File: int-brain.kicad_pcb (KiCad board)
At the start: 2 copper layers, 152.4 x 66.5 mm, 102 parts, among them J1 PWR, J10 Left, J11 Right, J12 1MA_ENC, J13 1MB_ENC, J14 2MA_ENC, J15 2MB_ENC, J16 USB_A, J2 UART0, J3 I2C0, J4 PWR, J5 1MA, J6 1MB, J7 2MA, J8 2MB, J9 MPU9250, SW1 SW_Push, U1 L298N, U2 ESP32-DevKitC, U3 L298N, U4 TPS5430DDA, U7 PCA9635, U8 TPS5430DDA

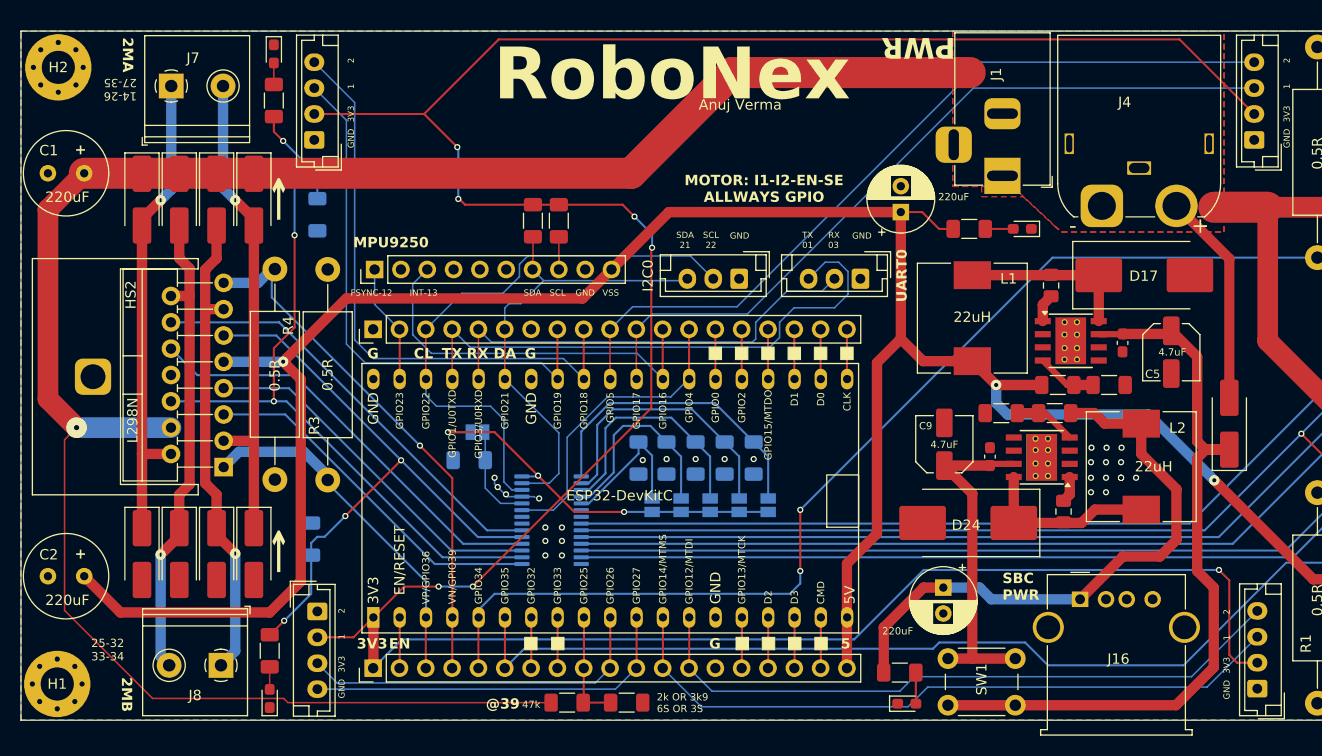
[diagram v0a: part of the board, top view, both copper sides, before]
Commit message: add cap to PCA ic
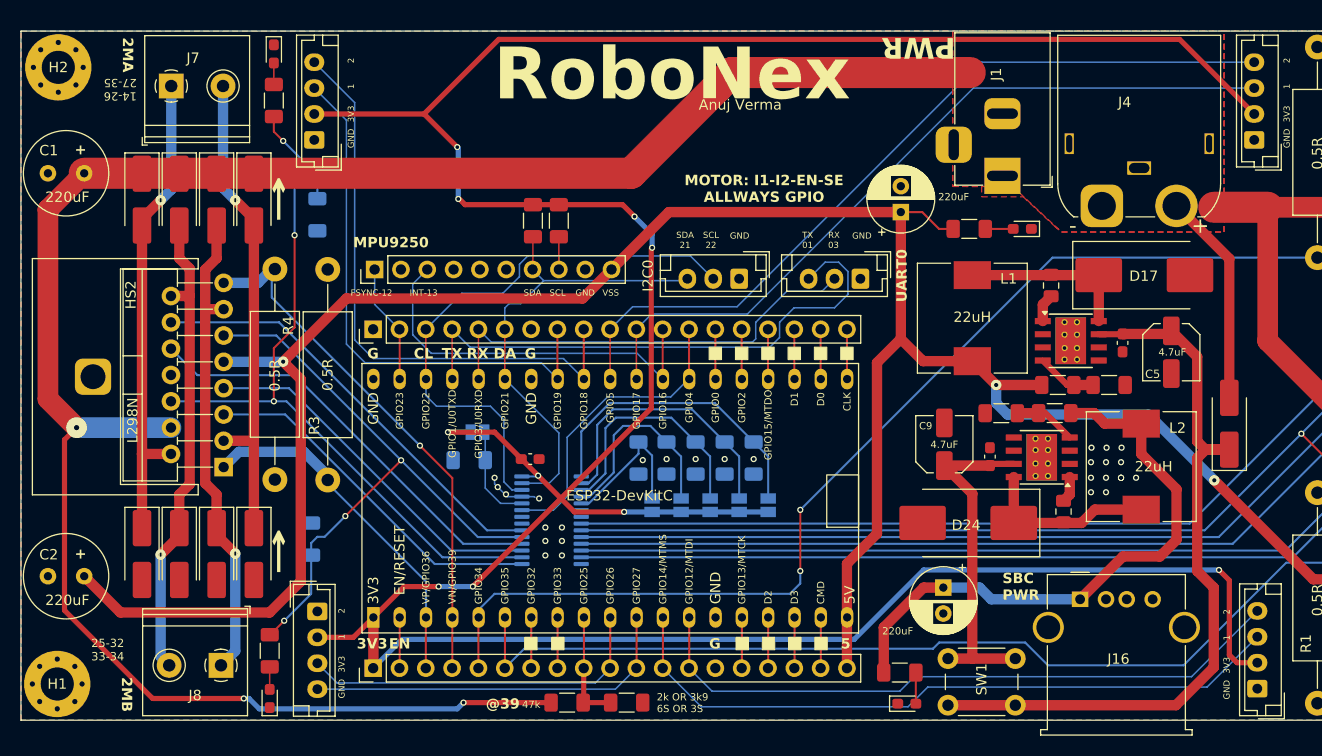
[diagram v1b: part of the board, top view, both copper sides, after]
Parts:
- added C13: 100nF, Capacitor_SMD:C_0603_1608Metric_Pad1.08x0.95mm_HandSolder, F.Cu at (167.0, 94.8)
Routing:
- net VS: track 290.8 -> 291.3 mm, vias 2 -> 4

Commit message: some zone
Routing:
- net VS: track 291.3 -> 289.0 mm
- net +3.3V: track 324.5 -> 322.6 mm
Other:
- outline, holes or cut-outs redrawn
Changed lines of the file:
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@@
 		(tags "capacitor handsolder")
 		(property "Reference" "C13"
-			(at 0 -1.43 360)
+			(at 0 -1.43 0)
 			(layer "F.SilkS")
 			(hide yes)
@@
 		)
 		(property "Value" "100nF"
-			(at 0 1.43 360)
+			(at 0 1.43 0)
 			(layer "F.Fab")
 			(effects
@@
 		)
 		(fp_text user "${REFERENCE}"
-			(at 0 0 360)
+			(at 0 0 0)
 			(layer "F.Fab")
 			(effects
@@
 		)
 		(property "Value" "1MA"
-			(at 8.95 -2.75 90)
+			(at 8.95 -1.9 90)
 			(unlocked yes)
 			(layer "F.SilkS" knockout)
@@
 		(layer "F.SilkS")
 	)
-	(gr_rect
-		(start 117.9 53.5)
-		(end 270.3 120)
+	(gr_arc
+		(start 268.3 53.5)
+		(mid 269.714214 54.085786)
+		(end 270.3 55.5)
+		(stroke
+			(width 0.05)
+			(type default)
+		)
+		(layer "Edge.Cuts")
+	)
+	(gr_line
+		(start 270.3 55.5)
+		(end 270.3 118)
+		(stroke
+			(width 0.05)
+			(type default)
+		)
+		(layer "Edge.Cuts")
+	)
+	(gr_line
+		(start 268.3 120)
+		(end 119.9 120)
+		(stroke
+			(width 0.05)
+			(type default)
+		)
+		(layer "Edge.Cuts")
+	)
+	(gr_line
+		(start 119.9 53.5)
+		(end 268.3 53.5)
+		(stroke
+			(width 0.05)
+			(type default)
+		)
+		(layer "Edge.Cuts")
+	)
+	(gr_arc
+		(start 119.9 120)
+		(mid 118.485786 119.414214)
+		(end 117.9 118)
+		(stroke
+			(width 0.05)
+			(type default)
+		)
+		(layer "Edge.Cuts")
+	)
+	(gr_line
+		(start 117.9 118)
+		(end 117.9 55.5)
+		(stroke
+			(width 0.05)
+			(type default)
+		)
+		(layer "Edge.Cuts")
+	)
+	(gr_arc
+		(start 270.3 118)
+		(mid 269.714214 119.414214)
+		(end 268.3 120)
+		(stroke
+			(width 0.05)
+			(type default)
+		)
+		(layer "Edge.Cuts")
+	)
+	(gr_arc
+		(start 117.9 55.5)
+		(mid 118.485786 54.085786)
+		(end 119.9 53.5)
 		(stroke
 			(width 0.05)
 			(type default)
 		)
-		(fill none)
 		(layer "Edge.Cuts")
 	)
@@
 	)
 	(segment
-		(start 186.5 57.5)
-		(end 209.5 57.5)
-		(width 3)
+		(start 160.6 118.3)
+		(end 169.05 118.3)
+		(width 0.5)
 		(layer "F.Cu")
 		(net 1)
@@
 	(segment
 		(start 176.78 67.22)
-		(end 185 59)
+		(end 184.4 59.6)
 		(width 3)
 		(layer "F.Cu")
@@
 	)
 	(segment
-		(start 160.6 118.3)
-		(end 169.05 118.3)
-		(width 0.5)
-		(layer "F.Cu")
-		(net 1)
-	)
-	(segment
 		(start 124 67.22)
 		(end 176.78 67.22)
@@
 	)
 	(segment
-		(start 185 59)
-		(end 186.5 57.5)
-		(width 3)
-		(layer "F.Cu")
-		(net 1)
-	)
-	(segment
 		(start 238.2 83.4)
 		(end 238.2 70.5)
@@
 	)
 	(segment
+		(start 184.4 59.6)
+		(end 208.1 59.6)
+		(width 3)
+		(layer "F.Cu")
+		(net 1)
+	)
+	(segment
 		(start 255.2 91.8)
 		(end 246.6 91.8)
@@
 	)
 	(segment
-		(start 236.9 61.5)
-		(end 229.7 54.3)
-		(width 0.5)
-		(layer "F.Cu")
-		(net 27)
-	)
-	(segment
 		(start 170 98.6)
 		(end 161.5 107.1)
@@
 	)
 	(segment
-		(start 229.7 54.3)
-		(end 164 54.3)
-		(width 0.5)
-		(layer "F.Cu")
-		(net 27)
-	)
-	(segment
 		(start 169.8 70.25)
 		(end 175.95 70.25)
@@
 	)
 	(segment
+		(start 161.7 56.6)
+		(end 156.8 61.5)
+		(width 0.5)
+		(layer "F.Cu")
+		(net 27)
+	)
+	(segment
 		(start 235.25 114.45)
 		(end 234.5 113.7)
@@
 	)
 	(segment
-		(start 159.1 92.2)
-		(end 163.6 92.2)
+		(start 236.9 61.5)
+		(end 232 56.6)
 		(width 0.5)
 		(layer "F.Cu")
@@
 	)
 	(segment
-		(start 160.75 70.25)
-		(end 169.8 70.25)
+		(start 159.1 92.2)
+		(end 163.6 92.2)
 		(width 0.5)
 		(layer "F.Cu")
@@
 	)
 	(segment
-		(start 164 54.3)
-		(end 156.8 61.5)
+		(start 160.75 70.25)
+		(end 169.8 70.25)
 		(width 0.5)
 		(layer "F.Cu")
@@
 		(width 0.5)
 		(layer "F.Cu")
+		(net 27)
+	)
+	(segment
+		(start 232 56.6)
+		(end 161.7 56.6)
+		(width 0.5)
+		(layer "F.Cu")

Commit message: add solder point for PCA I/O
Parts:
- added JP6: VCC, Jumper:SolderJumper-2_P1.3mm_Open_Pad1.0x1.5mm, F.Cu at (162.3, 99.0)
- added JP7: GND, Jumper:SolderJumper-2_P1.3mm_Open_Pad1.0x1.5mm, F.Cu at (159.5, 99.0)
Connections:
- U7 pad 25: GND -> /PCA_IO
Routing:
- net /PCA_IO: track 0.00 -> 6.82 mm, vias 0 -> 1
- net GND: track 5.20 -> 0.00 mm, vias 40 -> 36
- net +3.3V: track 322.6 -> 327.3 mm
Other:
- board text added: "PCA I/O"

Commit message: placed?
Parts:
- removed D11, D12, D13, D14, D15, D16, D23: D, Diode_SMD:D_SMA_Handsoldering
- removed D17, D24: B340, Diode_SMD:D_SMC_Handsoldering
- removed D18, D19, D20, D21: LED, LED_SMD:LED_0603_1608Metric_Pad1.05x0.95mm_HandSolder
- removed D22, D25: PWR, LED_SMD:LED_0603_1608Metric_Pad1.05x0.95mm_HandSolder
- removed HS1, HS2: Heatsink_Pad, heatsink:Heatsink_PI48
- removed JP0: A0, Jumper:SolderJumper-2_P1.3mm_Open_Pad1.0x1.5mm
- added C14: 220uF, Capacitor_SMD:CP_Elec_8x10.5, F.Cu at (47.8, 73.9)
- added C15: 4.7uF, Capacitor_SMD:CP_Elec_4x5.4, F.Cu at (96.6, 77.3)
- added C16: 4.7uF, Capacitor_SMD:C_0603_1608Metric_Pad1.08x0.95mm_HandSolder, B.Cu at (95.7, 79.2)
- added C17: 10nF, Capacitor_SMD:C_0805_2012Metric_Pad1.18x1.45mm_HandSolder, F.Cu at (104.4, 83.7)
- added C18: 330uF, Capacitor_SMD:CP_Elec_8x10.5, F.Cu at (73.2, 77.8)
- added C19: 10nF, Capacitor_SMD:C_0805_2012Metric_Pad1.18x1.45mm_HandSolder, B.Cu at (134.4, 131.8)
- added C20: 1uF, Capacitor_SMD:C_0805_2012Metric_Pad1.18x1.45mm_HandSolder, B.Cu at (134.4, 136.8)
- added C21: 220uF, Capacitor_SMD:CP_Elec_8x10.5, F.Cu at (119.1, 140.9)
- added C22: 10nF, Capacitor_SMD:C_0603_1608Metric_Pad1.08x0.95mm_HandSolder, B.Cu at (78.0, 132.7)
- added C23: 10nF, Capacitor_SMD:C_0603_1608Metric_Pad1.08x0.95mm_HandSolder, B.Cu at (97.6, 79.2)
- added C24: 10nF, Capacitor_SMD:C_0603_1608Metric_Pad1.08x0.95mm_HandSolder, F.Cu at (107.2, 131.4)
- added C25: 10nF, Capacitor_SMD:C_0603_1608Metric_Pad1.08x0.95mm_HandSolder, F.Cu at (67.8, 80.5)
- added J17: Conn_01x03, Connector_PinHeader_2.54mm:PinHeader_1x03_P2.54mm_Vertical, F.Cu at (63.3, 111.1)
- added R29: 10k, Resistor_SMD:R_1206_3216Metric_Pad1.30x1.75mm_HandSolder, F.Cu at (78.8, 100.0)
- added R30: 3k9, Resistor_SMD:R_1206_3216Metric_Pad1.30x1.75mm_HandSolder, F.Cu at (63.3, 116.0)
- added U10: ~, Package_SO:SOIC-8-1EP_3.9x4.9mm_P1.27mm_EP2.29x3mm_ThermalVias, F.Cu at (103.0, 79.5)
- added U11: DRV8251ADDAR, Package_SO:SOIC-8-1EP_3.9x4.9mm_P1.27mm_EP2.29x3mm_ThermalVias, B.Cu at (130.4, 135.3)
- added U12: INA139, Package_TO_SOT_SMD:SOT-23-5_HandSoldering, B.Cu at (125.3, 136.7)
- added U5: DRV8251ADDAR, Package_SO:SOIC-8-1EP_3.9x4.9mm_P1.27mm_EP2.29x3mm_ThermalVias, B.Cu at (132.2, 79.6)
- added U6: INA139, Package_TO_SOT_SMD:SOT-23-5_HandSoldering, B.Cu at (137.2, 78.3)
- added U9: INA139, Package_TO_SOT_SMD:SOT-23-5_HandSoldering, B.Cu at (62.7, 78.1)
- C1: value 220uF -> 100nF; footprint Capacitor_THT:C_Radial_D8.0mm_H11.5mm_P3.50mm -> Capacitor_SMD:C_0603_1608Metric_Pad1.08x0.95mm_HandSolder; moved to B.Cu
- C10: value 4.7uF -> 10nF; footprint Capacitor_SMD:C_0603_1608Metric_Pad1.08x0.95mm_HandSolder -> Capacitor_SMD:C_0805_2012Metric_Pad1.18x1.45mm_HandSolder
- C11: value 10nF -> 330uF; footprint Capacitor_SMD:C_0805_2012Metric_Pad1.18x1.45mm_HandSolder -> Capacitor_SMD:CP_Elec_8x10.5
- C12: value 220uF -> 10nF; footprint Capacitor_THT:CP_Radial_D6.3mm_P2.50mm -> Capacitor_SMD:C_0805_2012Metric_Pad1.18x1.45mm_HandSolder; moved to B.Cu
- C13: value 100nF -> 1uF; footprint Capacitor_SMD:C_0603_1608Metric_Pad1.08x0.95mm_HandSolder -> Capacitor_SMD:C_0805_2012Metric_Pad1.18x1.45mm_HandSolder; moved to B.Cu
- C2: value 220uF -> 10nF; footprint Capacitor_THT:C_Radial_D8.0mm_H11.5mm_P3.50mm -> Capacitor_SMD:C_0805_2012Metric_Pad1.18x1.45mm_HandSolder; moved to B.Cu
- C3: value 220uF -> 1uF; footprint Capacitor_THT:C_Radial_D8.0mm_H11.5mm_P3.50mm -> Capacitor_SMD:C_0805_2012Metric_Pad1.18x1.45mm_HandSolder; moved to B.Cu
- C4: footprint Capacitor_THT:C_Radial_D8.0mm_H11.5mm_P3.50mm -> Capacitor_SMD:CP_Elec_8x10.5
- C5: value 4.7uF -> 10nF; footprint Capacitor_SMD:C_Elec_5x5.8 -> Capacitor_SMD:C_0805_2012Metric_Pad1.18x1.45mm_HandSolder; moved to B.Cu
- C6: value 4.7uF -> 1uF; footprint Capacitor_SMD:C_0603_1608Metric_Pad1.08x0.95mm_HandSolder -> Capacitor_SMD:C_0805_2012Metric_Pad1.18x1.45mm_HandSolder; moved to B.Cu
- C7: value 10nF -> 220uF; footprint Capacitor_SMD:C_0805_2012Metric_Pad1.18x1.45mm_HandSolder -> Capacitor_SMD:CP_Elec_8x10.5
- C8: value 220uF -> 4.7uF; footprint Capacitor_THT:CP_Radial_D6.3mm_P2.50mm -> Capacitor_SMD:CP_Elec_4x5.4
- C9: footprint Capacitor_SMD:C_Elec_5x5.8 -> Capacitor_SMD:C_0603_1608Metric_Pad1.08x0.95mm_HandSolder; moved to B.Cu
- D1, D2, D3, D4: value D -> LED; footprint Diode_SMD:D_SMA_Handsoldering -> LED_SMD:LED_1206_3216Metric_Pad1.42x1.75mm_HandSolder
- D6, D7: value D -> PWR; footprint Diode_SMD:D_SMA_Handsoldering -> LED_SMD:LED_1206_3216Metric_Pad1.42x1.75mm_HandSolder
- D8, D9: value D -> SS54
- J1: value PWR -> Right; footprint Connector_BarrelJack:BarrelJack_Horizontal -> Connector_PinHeader_2.54mm:PinHeader_1x19_P2.54mm_Vertical
- J10: value Left -> 2MB; footprint Connector_PinHeader_2.54mm:PinHeader_1x19_P2.54mm_Vertical -> TerminalBlock_Philmore:TerminalBlock_Philmore_TB132_1x02_P5.00mm_Horizontal
- J11: value Right -> 1MB; footprint Connector_PinHeader_2.54mm:PinHeader_1x19_P2.54mm_Vertical -> TerminalBlock_Philmore:TerminalBlock_Philmore_TB132_1x02_P5.00mm_Horizontal
- J12: value 1MA_ENC -> 1MA; footprint Connector_JST:JST_EH_B4B-EH-A_1x04_P2.50mm_Vertical -> TerminalBlock_Philmore:TerminalBlock_Philmore_TB132_1x02_P5.00mm_Horizontal
- J13: value 1MB_ENC -> 1MA_ENC
- J14: value 2MA_ENC -> 1MB_ENC
- J15: value 2MB_ENC -> 2MA_ENC
- J16: value USB_A -> MPU9250; footprint Connector_USB:USB_A_Molex_67643_Horizontal -> Connector_PinHeader_2.54mm:PinHeader_1x10_P2.54mm_Vertical
- J2: value UART0 -> Left; footprint Connector_JST:JST_EH_B3B-EH-A_1x03_P2.50mm_Vertical -> Connector_PinHeader_2.54mm:PinHeader_1x19_P2.54mm_Vertical
- J3: value I2C0 -> PWR; footprint Connector_JST:JST_EH_B3B-EH-A_1x03_P2.50mm_Vertical -> Connector_BarrelJack:BarrelJack_Horizontal
- J5: value 1MA -> USB_A; footprint TerminalBlock_Philmore:TerminalBlock_Philmore_TB132_1x02_P5.00mm_Horizontal -> Connector_USB:USB_A_Molex_67643_Horizontal
- J6: value 1MB -> 2MB_ENC; footprint TerminalBlock_Philmore:TerminalBlock_Philmore_TB132_1x02_P5.00mm_Horizontal -> Connector_JST:JST_EH_B4B-EH-A_1x04_P2.50mm_Vertical
- J7: value 2MA -> I2C0; footprint TerminalBlock_Philmore:TerminalBlock_Philmore_TB132_1x02_P5.00mm_Horizontal -> Connector_JST:JST_EH_B3B-EH-A_1x03_P2.50mm_Vertical
- J8: value 2MB -> UART0; footprint TerminalBlock_Philmore:TerminalBlock_Philmore_TB132_1x02_P5.00mm_Horizontal -> Connector_JST:JST_EH_B3B-EH-A_1x03_P2.50mm_Vertical
- J9: value MPU9250 -> 2MA; footprint Connector_PinHeader_2.54mm:PinHeader_1x10_P2.54mm_Vertical -> TerminalBlock_Philmore:TerminalBlock_Philmore_TB132_1x02_P5.00mm_Horizontal
- JP1: value A1 -> A0
- JP2: value A2 -> A1
- JP3: value A3 -> A2
- JP4: value A4 -> A3
- JP5: value A5 -> A4
- JP6: value VCC -> A5; moved to B.Cu
- JP7: value GND -> VCC; moved to B.Cu
- R1, R2, R3: value 0.5R -> 220R; footprint Resistor_THT:R_Axial_DIN0414_L11.9mm_D4.5mm_P20.32mm_Horizontal -> Resistor_SMD:R_1206_3216Metric_Pad1.30x1.75mm_HandSolder
- R10: value 47k -> 3k9
- R12, R21: moved to F.Cu
- R13, R14: value 10k -> 470R; moved to F.Cu
- R15: value 10k -> 4.7k
- R16: moved to B.Cu
- R17: value 4.7k -> 10mR; footprint Resistor_SMD:R_1206_3216Metric_Pad1.30x1.75mm_HandSolder -> Resistor_SMD:R_2512_6332Metric_Pad1.40x3.35mm_HandSolder; moved to B.Cu
- R18, R20, R28: value 10k -> 24k
- R19: value 10k -> 10mR; footprint Resistor_SMD:R_1206_3216Metric_Pad1.30x1.75mm_HandSolder -> Resistor_SMD:R_2512_6332Metric_Pad1.40x3.35mm_HandSolder
- R22: value 10k -> 3.16k; moved to F.Cu
- R23: value 470R -> 10mR; footprint Resistor_SMD:R_1206_3216Metric_Pad1.30x1.75mm_HandSolder -> Resistor_SMD:R_2512_6332Metric_Pad1.40x3.35mm_HandSolder; moved to B.Cu
- R24: value 10k -> 24k; moved to B.Cu
- R25: value 3.24k -> 10k
- R26: value 10k -> 3.16k
- R27: value 3.24k -> 10mR; footprint Resistor_SMD:R_1206_3216Metric_Pad1.30x1.75mm_HandSolder -> Resistor_SMD:R_2512_6332Metric_Pad1.40x3.35mm_HandSolder; moved to B.Cu
- R4: value 0.5R -> 10k; footprint Resistor_THT:R_Axial_DIN0414_L11.9mm_D4.5mm_P20.32mm_Horizontal -> Resistor_SMD:R_1206_3216Metric_Pad1.30x1.75mm_HandSolder
- R6, R7: value 220R -> 10k
- R8: value 220R -> 47k
- R9: value 470R -> 10k
- U1: value L298N -> PCA9635; footprint Package_TO_SOT_THT:TO-220-15_P2.54x2.54mm_StaggerOdd_Lead4.58mm_Vertical -> Package_SO:TSSOP-28_4.4x9.7mm_P0.65mm; moved to B.Cu
- U2: footprint PCM_Espressif:ESP32-DevKitC -> PCM_Espressif:ESP32-DevKitC-slim
- U3: value L298N -> DRV8251ADDAR; footprint Package_TO_SOT_THT:TO-220-15_P2.54x2.54mm_StaggerOdd_Lead4.58mm_Vertical -> Package_SO:SOIC-8-1EP_3.9x4.9mm_P1.27mm_EP2.29x3mm_ThermalVias; moved to B.Cu
- U4: value TPS5430DDA -> INA139; footprint Package_SO:TI_SO-PowerPAD-8_ThermalVias -> Package_TO_SOT_SMD:SOT-23-5_HandSoldering; moved to B.Cu
- U7: value PCA9635 -> ~; footprint Package_SO:TSSOP-28_4.4x9.7mm_P0.65mm -> Package_SO:SOIC-8-1EP_3.9x4.9mm_P1.27mm_EP2.29x3mm_ThermalVias; moved to F.Cu
- U8: value TPS5430DDA -> DRV8251ADDAR; footprint Package_SO:TI_SO-PowerPAD-8_ThermalVias -> Package_SO:SOIC-8-1EP_3.9x4.9mm_P1.27mm_EP2.29x3mm_ThermalVias; moved to B.Cu
- moved J6 227.3 mm to (40.0, 142.4), turned to 90 degrees
- moved D5 223.0 mm to (42.6, 88.3), turned to 0 degrees
- moved C4 214.7 mm to (47.6, 140.9), turned to 90 degrees
- moved D2 208.1 mm to (51.7, 133.0), turned to 180 degrees
- moved D1 206.4 mm to (51.7, 81.7), turned to 0 degrees
- moved R2 205.6 mm to (45.6, 133.0), turned to 0 degrees
- moved D7 201.4 mm to (72.4, 139.3), turned to 180 degrees
- moved R1 198.0 mm to (45.7, 81.7), turned to 180 degrees
- moved H4 193.8 mm to (59.3, 94.0)
- moved C3 192.5 mm to (62.6, 136.8), turned to 90 degrees
- moved H3 189.9 mm to (59.9, 123.9)
- moved R14 188.0 mm to (67.0, 139.3), turned to 0 degrees
- moved U1 181.6 mm to (84.6, 109.7), turned to 180 degrees
- moved D8 180.6 mm to (83.1, 133.0)
- moved R12 178.6 mm to (76.1, 100.0), turned to -90 degrees
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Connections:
- C1 pad 1: GND -> +3.3V
- C1 pad 2: VS -> GND
- C10 pad 1: /buck2/BUCK_VIN -> Net-(U7-BOOT)
- C10 pad 2: GND -> /buck1/BUCK_OUT
- C11 pad 1: Net-(U8-BOOT) -> VSS
- C11 pad 2: /buck2/BUCK_OUT -> GND
- C12 pad 1: /buck2/VOUT -> +3.3V
- C13 pad 1: +3.3V -> VS
- C2 pad 1: GND -> +3.3V
- C2 pad 2: VSS -> GND
- C3 pad 1: GND -> VS
- C3 pad 2: VSS -> GND
- C4 pad 1: GND -> VS
- C4 pad 2: VS -> GND
- C5 pad 1: BUCK_VS -> +3.3V
- C6 pad 1: BUCK_VS -> VS
- C7 pad 1: Net-(U4-BOOT) -> VS
- C7 pad 2: /buck1/BUCK_OUT -> GND
- C8 pad 1: VSS -> VS
- C9 pad 1: /buck2/BUCK_VIN -> VS
- D1 pad 1: VS -> GND
- D1 pad 2: /1MA1 -> /1MAL
- D10 pad 1: /2MA1 -> VS
- D10 pad 2: GND -> /VS_UNSAFE
- D2 pad 1: /1MA1 -> GND
- D2 pad 2: GND -> /1MBL
- D3 pad 1: VS -> GND
- D3 pad 2: /1MA2 -> /2MAL
- D4 pad 1: /1MA2 -> GND
- D4 pad 2: GND -> /2MBL
- D5 pad 2: /1MB1 -> /VS_UNSAFE
- D6 pad 1: /1MB1 -> GND
- D6 pad 2: GND -> /PWR_LED_2
- D7 pad 1: VS -> GND
- D7 pad 2: /1MB2 -> /PWR_LED_1
- D8 pad 1: /1MB2 -> /buck1/BUCK_OUT
- D9 pad 1: VS -> /buck2/BUCK_OUT
- D9 pad 2: /2MA1 -> GND
- J1 pad 1: VS -> GND
- J1 pad 2: GND -> FSYNC
- J1 pad 3: (no net) -> SCL0
- J10 pad 1: +3.3V -> /2MB1
- J10 pad 2: /EN -> /2MB2
- J11 pad 1: GND -> /1MB1
- J11 pad 2: FSYNC -> /1MB2
- J12 pad 1: GND -> /1MA1
- J12 pad 2: +3.3V -> /1MA2
- J13 pad 3: /1MA1_ENC -> /2MA1_ENC
- J13 pad 4: /1MA2_ENC -> /2MA2_ENC
- J14 pad 3: /2MB1_ENC -> /1MA1_ENC
- J14 pad 4: /2MB2_ENC -> /1MA2_ENC
- J15 pad 3: /1MB1_ENC -> /2MB1_ENC
- J15 pad 4: /1MB2_ENC -> /2MB2_ENC
- J16 pad 1: /buck2/VOUT -> FSYNC
- J16 pad 3: unconnected-(J16-D+-Pad3) -> INT
- J16 pad 4: GND -> unconnected-(J16-Pin_4-Pad4)
- J16 pad 5: GND -> unconnected-(J16-Pin_5-Pad5)
- J2 pad 1: GND -> +3.3V
- J2 pad 2: /RX0 -> /EN
- J2 pad 3: /TX0 -> 2MB_SENSE
- J3 pad 1: GND -> /VS_UNSAFE
- J3 pad 2: SCL0 -> GND
- J3 pad 3: SDA0 -> GND
- J4 pad 2: VS -> /VS_UNSAFE
- J5 pad 1: /1MA1 -> /buck2/VOUT
- J5 pad 2: /1MA2 -> unconnected-(J5-D--Pad2)
- J6 pad 1: /1MB1 -> GND
- J6 pad 2: /1MB2 -> +3.3V
- J7 pad 1: /2MA1 -> GND
- J7 pad 2: /2MA2 -> SCL0
- J8 pad 1: /2MB1 -> GND
- J8 pad 2: /2MB2 -> /RX0
- J9 pad 1: FSYNC -> /2MA1
- J9 pad 2: unconnected-(J9-Pin_2-Pad2) -> /2MA2
- JP1 pad 2: /PCA_A1 -> /PCA_A0
- JP2 pad 2: /PCA_A2 -> /PCA_A1
- JP3 pad 2: /PCA_A3 -> /PCA_A2
- JP4 pad 2: /PCA_A4 -> /PCA_A3
- JP5 pad 2: /PCA_A5 -> /PCA_A4
- JP6 pad 2: /PCA_IO -> /PCA_A5
- JP7 pad 1: GND -> +3.3V
- R1 pad 1: 1MA_SENSE -> /1MA_EN
- R1 pad 2: GND -> /1MAL
- R10 pad 1: VS -> /3S
- R10 pad 2: VBATT -> GND
- R11 pad 1: VBATT -> GND
- R11 pad 2: GND -> /PCA_A4
- R12 pad 1: /1MA_EN -> GND
- R12 pad 2: GND -> /PCA_A5
- R13 pad 1: /2MA_EN -> /buck2/VOUT
- R13 pad 2: GND -> /PWR_LED_2
- R14 pad 1: /1MB_EN -> VSS
- R14 pad 2: GND -> /PWR_LED_1
- R15 pad 1: /2MB_EN -> SCL0
- R15 pad 2: GND -> +3.3V
- R16 pad 1: SCL0 -> SDA0
- R17 pad 1: SDA0 -> /motor-driver-2/IPROPI
- R17 pad 2: +3.3V -> GND
- R18 pad 1: GND -> 1MB_SENSE
- R18 pad 2: /PCA_A1 -> GND
- R19 pad 1: GND -> /motor-driver-3/IPROPI
- R19 pad 2: /PCA_A2 -> GND
- R2 pad 1: 1MB_SENSE -> /1MB_EN
- R2 pad 2: GND -> /1MBL
- R20 pad 1: GND -> 2MA_SENSE
- R20 pad 2: /PCA_A3 -> GND
- R21 pad 1: GND -> VSS
- R21 pad 2: /PCA_A4 -> /buck1/BUCK_VSENSE
- R22 pad 1: GND -> /buck1/BUCK_VSENSE
- R22 pad 2: /PCA_A5 -> GND
- R23 pad 1: /buck2/VOUT -> /motor-driver-1/IPROPI
- R23 pad 2: /PWR_LED_2 -> GND
- R24 pad 1: VSS -> 1MA_SENSE
- R24 pad 2: /buck1/BUCK_VSENSE -> GND
- R25 pad 1: /buck1/BUCK_VSENSE -> /buck2/VOUT
- R25 pad 2: GND -> /buck2/BUCK_VSENSE
- R26 pad 1: /buck2/VOUT -> /buck2/BUCK_VSENSE
- R26 pad 2: /buck2/BUCK_VSENSE -> GND
- R27 pad 1: /buck2/BUCK_VSENSE -> /motor-driver-4/IPROPI
- R28 pad 1: GND -> 2MB_SENSE
- R28 pad 2: /PCA_A0 -> GND
- R3 pad 1: 2MB_SENSE -> /2MA_EN
- R3 pad 2: GND -> /2MAL
- R4 pad 1: 2MA_SENSE -> GND
- R4 pad 2: GND -> /PCA_A0
- R5 pad 1: /1MA_EN -> /2MB_EN
- R5 pad 2: /1MAL -> /2MBL
- R6 pad 1: /1MB_EN -> GND
- R6 pad 2: /1MBL -> /PCA_A1
- R7 pad 1: /2MA_EN -> GND
- R7 pad 2: /2MAL -> /PCA_A2
- R8 pad 1: /2MB_EN -> VS
- R8 pad 2: /2MBL -> VBATT
- R9 pad 1: VSS -> GND
- R9 pad 2: /PWR_LED_1 -> /PCA_A3
- U1 pad 1: 1MA_SENSE -> /PCA_A0
- U1 pad 10: /1MB1_IN -> /2MA_IN1
- U1 pad 11: /1MB_EN -> /2MA_IN2
- U1 pad 12: /1MB2_IN -> /2MB_IN1
- U1 pad 13: /1MB1 -> /2MB_IN2
- U1 pad 14: /1MB2 -> GND
- U1 pad 15: 1MB_SENSE -> /1MB_IN1
- U1 pad 2: /1MA1 -> /PCA_A1
- U1 pad 3: /1MA2 -> /PCA_A2
- U1 pad 4: VS -> /PCA_A3
- U1 pad 5: /1MA1_IN -> /PCA_A4
- U1 pad 6: /1MA_EN -> /2MA_EN
- U1 pad 7: /1MA2_IN -> /2MB_EN
- U1 pad 8: GND -> unconnected-(U1-LED2-Pad8)
- U1 pad 9: VSS -> unconnected-(U1-LED3-Pad9)
- U3 pad 1: 2MB_SENSE -> /motor-driver-2/IPROPI
- U3 pad 2: /2MA1 -> /1MB_IN2
- U3 pad 3: /2MA2 -> /1MB_IN1
- U3 pad 4: VS -> +3.3V
- U3 pad 5: /2MA1_IN -> VS
- U3 pad 6: /2MA_EN -> /1MB1
- U3 pad 7: /2MA2_IN -> GND
- U3 pad 8: GND -> /1MB2
- U3 pad 9: VSS -> GND
- U4 pad 1: Net-(U4-BOOT) -> 1MB_SENSE
- U4 pad 2: unconnected-(U4-NC-Pad2) -> GND
- U4 pad 3: unconnected-(U4-NC-Pad3) -> /motor-driver-2/IPROPI
- U4 pad 4: /buck1/BUCK_VSENSE -> GND
- U4 pad 5: unconnected-(U4-EN-Pad5) -> +3.3V
- U7 pad 1: /PCA_A0 -> Net-(U7-BOOT)
- U7 pad 2: /PCA_A1 -> unconnected-(U7-NC-Pad2)
- U7 pad 3: /PCA_A2 -> unconnected-(U7-NC-Pad3)
- U7 pad 4: /PCA_A3 -> /buck1/BUCK_VSENSE
- U7 pad 5: /PCA_A4 -> unconnected-(U7-ENA-Pad5)
- U7 pad 6: unconnected-(U7-LED0-Pad6) -> GND
- U7 pad 7: unconnected-(U7-LED1-Pad7) -> VS
- U7 pad 8: /1MB2_IN -> /buck1/BUCK_OUT
- U7 pad 9: /1MB_EN -> GND
- U8 pad 1: Net-(U8-BOOT) -> /motor-driver-1/IPROPI
- U8 pad 2: unconnected-(U8-NC-Pad2) -> /1MA_IN2
- U8 pad 3: unconnected-(U8-NC-Pad3) -> /1MA_IN1
- U8 pad 4: /buck2/BUCK_VSENSE -> +3.3V
- U8 pad 5: unconnected-(U8-EN-Pad5) -> VS
- U8 pad 6: GND -> /1MA1
- U8 pad 7: /buck2/BUCK_VIN -> GND
- U8 pad 8: /buck2/BUCK_OUT -> /1MA2
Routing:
- net +3.3V: track 327.3 -> 0.00 mm, vias 10 -> 0
- net VS: track 289.0 -> 7.35 mm, vias 4 -> 1
- net VSS: track 266.0 -> 57.3 mm, vias 4 -> 0
- net /1MA_EN: track 130.7 -> 0.00 mm, vias 3 -> 0
- net 1MB_SENSE: track 128.5 -> 0.00 mm, vias 2 -> 0
- net /1MB_EN: track 127.7 -> 0.00 mm, vias 3 -> 0
- net 1MA_SENSE: track 121.2 -> 0.00 mm, vias 2 -> 0
- net /1MA2_IN: track 99.9 -> 0.00 mm
- net /1MA1_IN: track 99.4 -> 0.00 mm
- net /1MB2_IN: track 96.6 -> 0.00 mm
- net /1MB1_IN: track 96.1 -> 0.00 mm
- net /1MA2_ENC: track 77.6 -> 0.00 mm
- net /2MA_EN: track 74.1 -> 0.00 mm, vias 3 -> 0
- net /1MA1_ENC: track 74.1 -> 0.00 mm
- net BUCK_VS: track 73.7 -> 0.00 mm
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- added copper zone on F.Cu, net /buck1/BUCK_VSENSE
- added copper zone on F.Cu, net /buck2/BUCK_VSENSE
- removed copper zone on B.Cu, net GND
- removed copper zone on F.Cu, net GND
- removed copper zone on F.Cu, net VS
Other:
- board size 152.4 x 66.5 mm -> 103.2 x 79.5 mm
- board text removed: "+"
- board text removed: "1"
- board text removed: "14-26 27-35"
- board text removed: "16-5-17-15"
- board text removed: "18-23-19-4"
- board text removed: "2"
- board text removed: "25-32 33-34"
- board text removed: "2k OR 3k9 6S OR 3S"
- board text removed: "3V3"
- board text removed: "47k"
- board text removed: "5"
- board text removed: "@39"
- board text removed: "Anuj Verma"
- board text removed: "CL"
- board text removed: "DA"
- board text removed: "EN"
- board text removed: "FSYNC-12"
- board text removed: "G"
- board text removed: "GND"
- board text removed: "INT-13"
- board text removed: "MOTOR: I1-I2-EN-SE ALLWAYS GPIO"
- board text removed: "PCA I/O"
- board text removed: "RX"
- board text removed: "RX 03"
- board text removed: "RoboNex"
- board text removed: "SBC PWR"
- board text removed: "SCL"
- board text removed: "SCL 22"
- board text removed: "SDA"
- board text removed: "SDA 21"
- board text removed: "TX"
- board text removed: "TX 01"
- board text removed: "VSS"
- board text removed: "→"

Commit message: traced
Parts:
- added C26: 10uF, Capacitor_SMD:C_1206_3216Metric_Pad1.33x1.80mm_HandSolder, F.Cu at (95.1, 111.6)
- added C27: 10uF, Capacitor_SMD:C_1206_3216Metric_Pad1.33x1.80mm_HandSolder, F.Cu at (109.8, 109.2)
- added U13: AMS1117-3.3, Package_TO_SOT_SMD:SOT-223-3_TabPin2, F.Cu at (102.6, 109.3)
- moved SW1 50.0 mm to (80.8, 69.8), turned to 0 degrees
- moved R15 17.6 mm to (84.0, 137.4)
- moved R16 16.8 mm to (81.5, 137.4)
- moved R8 6.92 mm to (58.3, 108.5)
- moved D2 6.25 mm to (45.5, 133.2), turned to 0 degrees
- moved D1 6.05 mm to (45.6, 81.7)
- moved R2 5.95 mm to (51.5, 133.2), turned to 180 degrees
- moved R1 5.95 mm to (51.6, 81.7)
- moved J16 4.91 mm to (66.2, 142.0)
- moved D5 4.15 mm to (38.5, 88.3)
- moved J3 3.80 mm to (47.9, 96.2)
- moved J4 3.80 mm to (50.8, 116.3)
- moved D10 3.71 mm to (38.5, 124.1)
- moved H1 3.08 mm to (119.7, 123.1)
- moved D6 2.60 mm to (134.4, 110.6)
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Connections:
- J1 pad 10: /1MA2_ENC -> /2MA1_ENC
- J1 pad 11: /1MA1_ENC -> /2MA2_ENC
- J1 pad 12: INT -> /GPIO16
- J1 pad 2: FSYNC -> /GPIO23
- J1 pad 8: /2MA1_ENC -> /1MA2_ENC
- J1 pad 9: /2MA2_ENC -> /1MA1_ENC
- J2 pad 1: +3.3V -> +3.3VA
- J2 pad 10: /2MB1_ENC -> /1MB2_ENC
- J2 pad 11: /2MB2_ENC -> /1MB1_ENC
- J2 pad 12: /1MB1_ENC -> /2MB1_ENC
- J2 pad 13: /1MB2_ENC -> /2MB2_ENC
- J2 pad 7: /GPIO32 -> FSYNC
- J2 pad 8: /GPIO33 -> INT
- SW1 pad 1: BUCK_VS -> VS
- U1 pad 10: /2MA_IN1 -> /2MA_IN2
- U1 pad 11: /2MA_IN2 -> /2MB_IN1
- U1 pad 12: /2MB_IN1 -> /2MB_IN2
- U1 pad 13: /2MB_IN2 -> /2MB_EN
- U1 pad 17: /1MA_IN1 -> /1MB_EN
- U1 pad 18: /1MA_IN2 -> /1MA_EN
- U1 pad 19: unconnected-(U1-LED12-Pad19) -> /1MA_IN1
- U1 pad 20: unconnected-(U1-LED13-Pad20) -> /1MA_IN2
- U1 pad 21: /1MB_EN -> unconnected-(U1-LED14-Pad21)
- U1 pad 22: /1MA_EN -> unconnected-(U1-LED15-Pad22)
- U1 pad 6: /2MA_EN -> unconnected-(U1-LED0-Pad6)
- U1 pad 7: /2MB_EN -> unconnected-(U1-LED1-Pad7)
- U1 pad 8: unconnected-(U1-LED2-Pad8) -> /2MA_EN
- U1 pad 9: unconnected-(U1-LED3-Pad9) -> /2MA_IN1
- U2 pad 1: +3.3V -> +3.3VA
- U2 pad 10: /2MB1_ENC -> /1MB2_ENC
- U2 pad 11: /2MB2_ENC -> /1MB1_ENC
- U2 pad 12: /1MB1_ENC -> /2MB1_ENC
- U2 pad 13: /1MB2_ENC -> /2MB2_ENC
- U2 pad 27: INT -> /GPIO16
- U2 pad 28: /1MA1_ENC -> /2MA2_ENC
- U2 pad 29: /1MA2_ENC -> /2MA1_ENC
- U2 pad 30: /2MA2_ENC -> /1MA1_ENC
- U2 pad 31: /2MA1_ENC -> /1MA2_ENC
- U2 pad 37: FSYNC -> /GPIO23
- U2 pad 7: /GPIO32 -> FSYNC
- U2 pad 8: /GPIO33 -> INT
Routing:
- net VS: track 7.35 -> 456.3 mm, vias 1 -> 6
- net +3.3V: track 0.00 -> 377.3 mm, vias 0 -> 10
- net SCL0: track 0.00 -> 171.9 mm, vias 0 -> 7
- net SDA0: track 0.00 -> 150.7 mm, vias 0 -> 3
- net 2MA_SENSE: track 0.00 -> 116.8 mm, vias 0 -> 7
- net /TX0: track 0.00 -> 77.0 mm, vias 0 -> 3
- net /RX0: track 0.00 -> 75.8 mm, vias 0 -> 3
- net /2MA_IN2: track 0.00 -> 75.1 mm
- net /2MA_IN1: track 0.00 -> 73.5 mm
- net 2MB_SENSE: track 0.00 -> 66.8 mm, vias 0 -> 1
- net /1MB1_ENC: track 0.00 -> 65.8 mm, vias 0 -> 1
- net /1MB2_ENC: track 0.00 -> 61.9 mm, vias 0 -> 1
- net /1MA1_ENC: track 0.00 -> 58.1 mm, vias 0 -> 2
- net /2MB_IN1: track 0.00 -> 55.2 mm
- net /1MA2_ENC: track 0.00 -> 54.7 mm, vias 0 -> 2
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- added copper zone on F.Cu, net +3.3V
- added copper zone on F.Cu, net /VS_UNSAFE
- added copper zone on F.Cu, net /buck2/VOUT
- added copper zone on B.Cu, net GND
- added copper zone on F.Cu, net GND
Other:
- board size 103.2 x 79.5 mm -> 107 x 79.5 mm

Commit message: done?
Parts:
- added R31: 10k, Resistor_SMD:R_1206_3216Metric_Pad1.30x1.75mm_HandSolder, B.Cu at (87.4, 100.1)
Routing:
- net /buck2/BUCK_VIN: track 28.3 -> 26.8 mm
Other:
- board text added: "2 1"
- board text added: "2 1 3V3 GND"
- board text added: "3S"
- board text added: "3V3"
- board text added: "5V"
- board text added: "6S"
- board text added: "A0"
- board text added: "A1"
- board text added: "A2"
- board text added: "A3"
- board text added: "A4"
- board text added: "A5"
- board text added: "DA"
- board text added: "EN"
- board text added: "G"
- board text added: "GND 3V3 1 2"
- board text added: "I/O"
- board text added: "MOTOR 1MA [12 13 11]"
- board text added: "MOTOR 1MB [8 9 10]"
- board text added: "MOTOR 2MA [3 4 2]"
- board text added: "MOTOR 2MB [5 6 7]"
- board text added: "PCA I2C ADDRESS"
- board text added: "POWER 12V / 24V"
- board text added: "RX"
- board text added: "SBC PWR 5VDC 5A"
- board text added: "SBC PWR ON/OFF"
- board text added: "SC"
- board text added: "SDA SCL GND"
- board text added: "TX"
- board text added: "TX RX GND"

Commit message: minor improvements
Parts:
- J1: value Right -> Top
- J17: value Conn_01x03 -> VBATT_SELECT
- J2: value Left -> Bottom
- JP7: value VCC -> I/O
- R30: value 3k9 -> 2k
- U10, U7: value ~ -> TPS5450DDA
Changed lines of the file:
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@@
 			(outputformat 1)
 			(mirror no)
-			(drillshape 1)
+			(drillshape 0)
 			(scaleselection 1)
-			(outputdirectory "")
+			(outputdirectory "exports/gerbers/")
 		)
 	)
@@
 			)
 		)
-		(property "Value" "Left"
+		(property "Value" "Bottom"
 			(at 0 48.05 90)
 			(layer "F.Fab")
@@
 			)
 		)
-		(property "Value" "~"
+		(property "Value" "TPS5450DDA"
 			(at 0 3.4 0)
 			(layer "F.Fab")
@@
 			)
 		)
-		(property "Datasheet" ""
+		(property "Datasheet" "https://www.ti.com/lit/gpn/TPS5450"
 			(at 0 0 180)
 			(unlocked yes)
@@
 			)
 		)
-		(property "Description" ""
+		(property "Description" "TPS5450 5-A, Wide Input Range, Step-Down Converter"
 			(at 0 0 180)
 			(unlocked yes)
@@
 			)
 		)
-		(property "Value" "3k9"
+		(property "Value" "2k"
 			(at 0 1.82 90)
 			(layer "F.Fab")
@@
 			)
 		)
-		(property "Value" "Conn_01x03"
+		(property "Value" "VBATT_SELECT"
 			(at 0 7.41 0)
 			(layer "F.Fab")
@@
 			)
 		)
-		(property "Value" "Right"
+		(property "Value" "Top"
 			(at 0 48.05 90)
 			(layer "F.Fab")
@@
 			)
 		)
-		(property "Value" "~"
+		(property "Value" "TPS5450DDA"
 			(at 0 3.4 0)
 			(layer "F.Fab")
@@
 			)
 		)
-		(property "Datasheet" ""
+		(property "Datasheet" "https://www.ti.com/lit/gpn/TPS5450"
 			(at 0 0 0)
 			(unlocked yes)
@@
 			)
 		)
-		(property "Description" ""
+		(property "Description" "TPS5450 5-A, Wide Input Range, Step-Down Converter"
 			(at 0 0 0)
 			(unlocked yes)
@@
 			)
 		)
-		(property "Value" "VCC"
+		(property "Value" "I/O"
 			(at 0 -1.9 90)
 			(layer "B.Fab")
